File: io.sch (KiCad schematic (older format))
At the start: 5 parts, among them J2 Connector_1, J3 Uart, J4 Connector_2, U4 USBLC6-2SC6

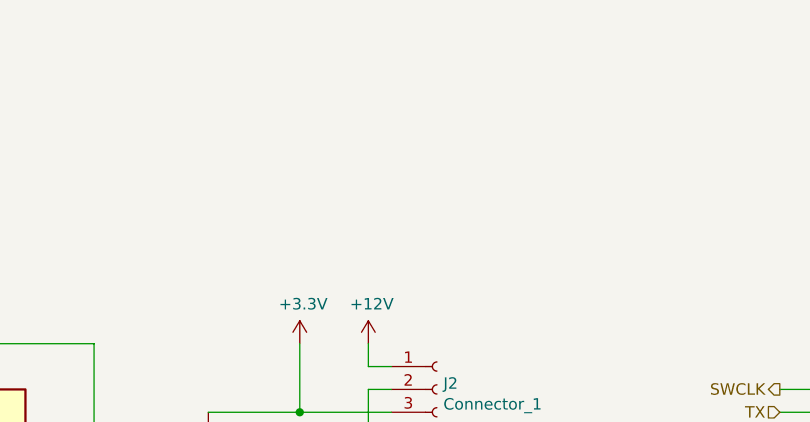
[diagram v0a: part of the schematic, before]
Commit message: Added an optional power output header Changed the resistors for the VCNT2020 to improve performance
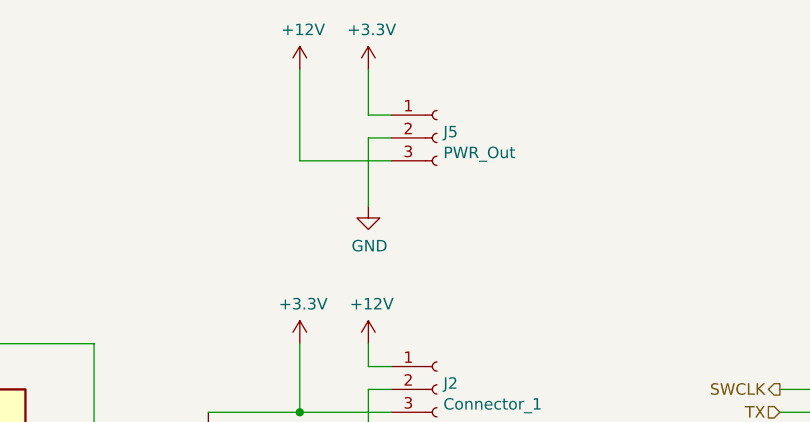
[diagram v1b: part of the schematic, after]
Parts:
- added J5: PWR_Out, Connector_PinSocket_1.27mm:PinSocket_1x03_P1.27mm_Vertical_SMD_Pin1Left, symbol Connector:Conn_01x03_Female
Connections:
- net +12V: now also J5.3 (Pin_3)
- net +3V3: now also J5.1 (Pin_1)
- net GND: now also J5.2 (Pin_2)
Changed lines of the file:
@@
 Sheet 4 6
 Title "MiniFeed"
-Date "2021-01-17"
+Date "2021-02-25"
 Rev "1.0"
 Comp "SG-O"
@@
 Text HLabel 7700 3100 0    50   Output ~ 0
 SWCLK
+$Comp
+L Connector:Conn_01x03_Female J5
+U 1 1 60249810
+P 6200 2000
+F 0 "J5" H 6228 2026 50  0000 L CNN
+F 1 "PWR_Out" H 6228 1935 50  0000 L CNN
+F 2 "Connector_PinSocket_1.27mm:PinSocket_1x03_P1.27mm_Vertical_SMD_Pin1Left" H 6200 2000 50  0001 C CNN
+F 3 "~" H 6200 2000 50  0001 C CNN
+F 4 "DNP" H 6200 2000 50  0001 C CNN "DNP"
+	1    6200 2000
+	1    0    0    -1
+$EndComp
+Wire Wire Line
+	5900 1900 5900 1700
+$Comp
+L power:+3.3V #PWR?
+U 1 1 6024A394
+P 5900 1700
+AR Path="/6024A394" Ref="#PWR?"  Part="1"
+AR Path="/60234D6B/6024A394" Ref="#PWR046"  Part="1"
+F 0 "#PWR046" H 5900 1550 50  0001 C CNN
+F 1 "+3.3V" H 5915 1873 50  0000 C CNN
+F 2 "" H 5900 1700 50  0001 C CNN
+F 3 "" H 5900 1700 50  0001 C CNN
+	1    5900 1700
+	1    0    0    -1
+$EndComp
+$Comp
+L power:+12V #PWR?
+U 1 1 6024B159
+P 5600 1700
+AR Path="/6024B159" Ref="#PWR?"  Part="1"
+AR Path="/60234D6B/6024B159" Ref="#PWR045"  Part="1"
+F 0 "#PWR045" H 5600 1550 50  0001 C CNN
+F 1 "+12V" H 5615 1873 50  0000 C CNN
+F 2 "" H 5600 1700 50  0001 C CNN
+F 3 "" H 5600 1700 50  0001 C CNN
+	1    5600 1700
+	1    0    0    -1
+$EndComp
+Wire Wire Line
+	6000 1900 5900 1900
+Wire Wire Line
+	6000 2100 5600 2100
+Wire Wire Line
+	5600 1700 5600 2100
+Wire Wire Line
+	6000 2000 5900 2000
+Wire Wire Line
+	5900 2000 5900 2300
+$Comp
+L power:GND #PWR?
+U 1 1 6024F207
+P 5900 2300
+AR Path="/6024F207" Ref="#PWR?"  Part="1"
+AR Path="/60234D6B/6024F207" Ref="#PWR047"  Part="1"
+F 0 "#PWR047" H 5900 2050 50  0001 C CNN
+F 1 "GND" H 5905 2127 50  0000 C CNN
+F 2 "" H 5900 2300 50  0001 C CNN
+F 3 "" H 5900 2300 50  0001 C CNN
+	1    5900 2300
+	1    0    0    -1
+$EndComp
 $EndSCHEMATC
